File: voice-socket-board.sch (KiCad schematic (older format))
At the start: 258 parts

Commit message: changes
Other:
- note removed: "WHY IS THIS OP AMP FLIPPED OVER????"
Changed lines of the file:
@@
 F 3 "~" H 3775 14550 60  0000 C CNN
 	2    3775 14550
-	1    0    0    1
+	1    0    0    -1
 $EndComp
 $Comp
@@
 Wire Wire Line
 	20875 10525 20875 10625
-Text Notes 3650 14875 0    50   ~ 0
-WHY IS THIS OP AMP FLIPPED OVER????
 $Comp
 L R_US R?

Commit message: updated with new voice card pinout, sub oscillator added. Need to add LFO LED circuit
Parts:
- removed J?: DDR3-DIMM, MyModules:DDR3-DIMM-MO-269, symbol DDR3-DIMM
- removed R?: 10K, symbol R_US
- removed U?: CD4024BE, DIP254P762X508-14, symbol CD4024BE
- removed U?: CD4013BE, DIP254P762X508-14, symbol CD4013BE
- added C?: 0.1μ, symbol C_US
- added C?: 10p, ~, symbol C_US
- added D? (x2): 1N4148, ~, symbol DIODE
- added J?: DDR3-DIMM, MyModules:DDR3-DIMM-MO-269, symbol DDR3-DIMM
- added Q?: MMBT3904, SOT-23, symbol MMBT3904
- added R? (x2): 4.7K, symbol R_US
- added R?: 100K, ~, symbol R_US
- added R?: 68K, symbol R_US
- added R?: 220K, symbol R_US
- added R?: 33K, symbol R_US
- added R? (x2): 47K, symbol R_US
- added SW?: SP3T, symbol SP3T
- added U? (x2): 4013, symbol 4013
- added VR?: 50K, symbol POT_US
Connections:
- net labels added: 1_OCT_DOWN_SQUARE, 2_OCT_DOWN_PULSE, 2_OCT_DOWN_SQUARE, SUB_OSC
- wire segments 558 -> 723
- no-connect marks 17 -> 10
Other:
- note added: "EG2 POL"
- note added: "Ian Fritz Super Sampe & Hold"
- note added: "MIXER"
- note added: "NEED TO BREADBOARD SUB OSCILLATOR"
- note added: "QUICK & DIRTY DEBOUNCE\n"
- note added: "SH101 SUB OSCILLATOR FROM:\nhttp://electro-music.com/forum/topic-18983.html"
- note added: "SYNC SWITCH"
- note removed: "6 VPP"
- note removed: "Changed to 47K to\nprevent clipping"
- moved on the sheet: C?, R?, VR?

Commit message: added a few notes, plus LFO LED circuit
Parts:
- added D?: LED, symbol LED
- added Q?: MMBT3904, SOT-23, symbol MMBT3904
- added R?: 47K, symbol R_US
- added R?: 1K, symbol R_US
- U? (x2): value TL072- -> LM833
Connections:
- wire segments 723 -> 731
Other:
- note added: "NEED TO BREADBOARD SUB OSCILLATOR\nIT WILL HAVE +5V DC OFFSET. WILL THIS BE \nBLOCKED BY POST MIXER BLOCKING CAP?"
- note added: "OR SOME OTHER LOW OFFSET PRECISION OP AMP"
- note removed: "NEED TO BREADBOARD SUB OSCILLATOR"
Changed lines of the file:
@@
 P 13350 5775
 F 0 "U?" H 13300 5975 60  0000 L CNN
-F 1 "TL072-" H 13300 5525 60  0000 L CNN
+F 1 "LM833" H 13300 5525 60  0000 L CNN
 F 2 "" H 13350 5775 60  0000 C CNN
 F 3 "" H 13350 5775 60  0000 C CNN
@@
 P 10250 6200
 F 0 "U?" H 10200 6400 60  0000 L CNN
-F 1 "TL072-" H 10200 5950 60  0000 L CNN
+F 1 "LM833" H 10200 5950 60  0000 L CNN
 F 2 "" H 10250 6200 60  0000 C CNN
 F 3 "" H 10250 6200 60  0000 C CNN
@@
 Connection ~ 34375 7150
 Text Notes 31375 6550 0    60   ~ 0
-NEED TO BREADBOARD SUB OSCILLATOR
+NEED TO BREADBOARD SUB OSCILLATOR\nIT WILL HAVE +5V DC OFFSET. WILL THIS BE \nBLOCKED BY POST MIXER BLOCKING CAP?
 Text Notes 30875 8575 0    60   ~ 0
 SH101 SUB OSCILLATOR FROM:\nhttp://electro-music.com/forum/topic-18983.html
@@
 Wire Wire Line
 	30825 7075 30825 7100
+$Comp
+L R_US R?
+U 1 1 56680CC3
+P 21425 13100
+F 0 "R?" V 21505 13100 50  0000 C CNN
+F 1 "47K" V 21345 13100 50  0000 C CNN
+F 2 "" H 21425 13100 60  0000 C CNN
+F 3 "" H 21425 13100 60  0000 C CNN
+	1    21425 13100
+	0    1    1    0
+$EndComp
+$Comp
+L R_US R?
+U 1 1 56680CCA
+P 22175 12650
+F 0 "R?" V 22255 12650 50  0000 C CNN
+F 1 "1K" V 22095 12650 50  0000 C CNN
+F 2 "" H 22175 12650 60  0000 C CNN
+F 3 "" H 22175 12650 60  0000 C CNN
+	1    22175 12650
+	0    -1   -1   0
+$EndComp
+$Comp
+L GND_E #PWR?
+U 1 1 56680CD1
+P 23025 12950
+F 0 "#PWR?" V 23025 12950 30  0001 C CNN
+F 1 "GND_E" H 23025 12880 30  0001 C CNN
+F 2 "~" H 23025 12950 60  0000 C CNN
+F 3 "~" H 23025 12950 60  0000 C CNN
+	1    23025 12950
+	1    0    0    -1
+$EndComp
+Wire Wire Line
+	21575 12650 21425 12650
+Wire Wire Line
+	23025 12650 23025 12950
+Wire Wire Line
+	22825 12650 23025 12650
+Wire Wire Line
+	21775 13100 21775 12950
+Wire Wire Line
+	21625 13100 21775 13100
+Wire Wire Line
+	21225 13100 21125 13100
+Wire Wire Line
+	21425 12650 21425 12450
+$Comp
+L MMBT3904 Q?
+U 1 1 566845D9
+P 21775 12750
+F 0 "Q?" H 21975 12825 50  0000 L CNN
+F 1 "MMBT3904" H 21975 12750 50  0000 L CNN
+F 2 "SOT-23" H 21975 12675 50  0001 L CIN
+F 3 "" H 21775 12750 50  0000 L CNN
+	1    21775 12750
+	0    -1   -1   0
+$EndComp
+$Comp
+L LED D?
+U 1 1 56688E5A
+P 22625 12650
+F 0 "D?" H 22625 12750 50  0000 C CNN
+F 1 "LED" H 22625 12550 50  0000 C CNN
+F 2 "" H 22625 12650 60  0000 C CNN
+F 3 "" H 22625 12650 60  0000 C CNN
+	1    22625 12650
+	-1   0    0    1
+$EndComp
+Wire Wire Line
+	22375 12650 22425 12650
+$Comp
+L +12V #PWR?
+U 1 1 56691909
+P 21425 12450
+F 0 "#PWR?" H 21425 12300 50  0001 C CNN
+F 1 "+12V" H 21425 12590 50  0000 C CNN
+F 2 "" H 21425 12450 60  0000 C CNN
+F 3 "" H 21425 12450 60  0000 C CNN
+	1    21425 12450
+	-1   0    0    -1
+$EndComp
+Connection ~ 9750 6200
+Text Notes 13400 6150 0    50   ~ 0
+OR SOME OTHER LOW OFFSET PRECISION OP AMP
 $EndSCHEMATC

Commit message: just made DDR3 DIMM connector footprint. 240 pins. Phew.
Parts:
- removed C? (x2): 470n, ~, symbol C_US
- removed C?: 0.1μ, symbol C_US
- removed J?: JACK_MONO_SW, symbol JACK_MONO_SW
- removed Q?: BCM857BS, ~, symbol BCM857BS
- removed R? (x4): 4.7K, ~, symbol R_US
- removed R? (x2): 100K, symbol R_US
- removed R?: 39K, ~, symbol R_US
- removed R?: 33K, symbol R_US
- removed R?: 1K 3300ppm/K, ~, symbol R_TEMPCO
- removed R? (x2): 4.7K, symbol R_US
- removed SW? (x2): SPST, symbol SPST
- removed TP? (x2): CONN_1, ~, symbol CONN_1
- removed U? (x2): LM13700, ~, symbol LM13700
- removed U? (x2): TL072-, ~, symbol TL072-
- removed VR?: 50K, symbol POT_US
- added C?: 470n, ~, symbol C_US
- added C? (x2): 10μF, MyModules:2MM-POL-CAP, symbol CP_US
- added C? (x10): 100n, MyModules:SM0603-C-JRL, symbol C_US
- added J?: JACK_MONO_SW, symbol JACK_MONO_SW
- added P? (x2): CONN_01X03, symbol CONN_01X03
- added P?: CONN_02X05, Pin_Headers:Pin_Header_Straight_2x05, symbol CONN_02X05
- added R?: 100K, symbol R_US
- added R? (x6): 47K, symbol R_US
- added R?: 1meg, symbol R_US
- added R? (x2): 100, symbol R_US
- added R?: 10K, symbol R_US
- added SW?: SP3T, symbol SP3T
- added SW? (x2): SPST, symbol SPST
- added TP?: CONN_1, ~, symbol CONN_1
- added U? (x2): TL072-, ~, symbol TL072-
- added U? (x2): TL072-, symbol TL072-
- added VR?: 1meg LOG, symbol POT_US
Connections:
- net labels added: KEY_TRACK
- wire segments 731 -> 1002
- no-connect marks 10 -> 8
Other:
- note added: "DECOUPLING"
- note added: "JUMPER"
- note added: "NORM"
- note added: "SIMPLE SLEW FROM:\nhttp://4.bp.blogspot.com/_UZMTRL9r8vU/TTGv3KWKT1I/AAAAAAAAAGw/SQU2PrACBgo/s1600/slew.jpg\nhttp://synovatron.blogspot.co.uk/p/cv-tools-project.html"
- note added: "VCF KEY\nTRACKING\n"
- note added: "WIDE"
- note removed: "*NOTE: C47 and C48 values: need\nto experiment more with C47 and \nC48 values. Changee to dual\nfootprint 0805 and TH."
- note removed: "ADAPTED FROM SCI PROPHET 5 GLIDE CIRCUIT"
- note removed: "GLIDE\n"
- moved on the sheet: R?

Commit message: annotated, doing ERC now
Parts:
- removed J?: JACK_MONO_SW, symbol JACK_MONO_SW
- removed Q? (x2): DMMT3904, symbol DMMT3904
- removed R?: 10K, symbol R_US
- removed VR?: POT_US, symbol POT_US
- added Q2: DMMT3904W, SOT-23, symbol DMMT3904W
- added R12, R7: 100K, symbol R_US
- gave numbers to parts that had none: 273
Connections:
- net +12V: no longer U5.8 (V+)
- net -12V: no longer U5.4 (V-)
- net VCO1_OCTAVE: now also R7.2
- net VCO1_PITCH_CV: now also R13.1, R12.1, R7.1
- net VCO2_OCTAVE: now also R12.2
- net at D3.2 (K), R58.2, R59.1: now also U4.3 (+); no longer U4.5 (+)
- net at R56.1, R57.1: now also U4.2 (-); no longer U4.6 (-)
- net at D5.1 (A), Q3.2 (G), Q3.5 (G): now also U4.1; no longer U4.7
- net at C16.2, R63.1: now also Q2.5 (E)
- net at C18.1 (+), R65.1: now also Q2.3 (C)
- net at C17.1 (+), R66.1: now also Q2.4 (E)
- net at R62.2: now also U5.6 (-); no longer U5.2 (-)
- net at P2.3 (P3), R60.1: now also U5.7; no longer U5.1
- net at R54.2, R55.2: now also U5.5 (+); no longer U5.3 (+)
- net 1_OCT_DOWN_SQUARE: no longer names the net of D7.1 (A), R83.2, SW10.1
- net 2_OCT_DOWN_PULSE: no longer names the net of D6.2 (K), D7.2 (K), SW10.4
- net 2_OCT_DOWN_SQUARE: no longer names the net of D6.1 (A), R82.2, SW10.2
- new net: Q2.1 (B), Q2.2 (B)
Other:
- note added: "1_OCT_DOWN_SQUARE"
- note added: "2_OCT_DOWN_PULSE"
- note added: "2_OCT_DOWN_SQUARE"
- moved on the sheet: C1, C10, C11, C12, C13, C14, C15, C16, C17, C18, C19, C2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

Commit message: starting footprint assignment. added .gitingore
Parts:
- removed U10: TL074-, ~, symbol TL074-
- added unit 2 of U10
- VR10: renamed from VR16; value POT_US -> 50K
- VR11: renamed from VR17; value POT_US -> 50K
- VR12: renamed from VR18; value POT_US -> 50K
- VR13: renamed from VR19; value POT_US -> 50K
- VR14: renamed from VR20; value POT_US -> 50K
- VR7: renamed from VR13; value POT_US -> 50K
- VR8: renamed from VR14; value POT_US -> 50K
- VR9: renamed from VR15; value POT_US -> 50K
- renumbered J4 to J2, J2 to P4, VR6 to TR4, VR8 to TR5, VR7 to TR6, VR9 to TR7, VR10 to TR8, VR11 to TR9, U11 to U10, U12 to U11, VR21 to VR15, VR22 to VR16, VR25 to VR17, VR27 to VR18, VR26 to VR19, VR28 to VR20, VR23 to VR21, VR24 to VR22, VR29 to VR23, VR30 to VR24, VR31 to VR25, VR32 to VR26, VR12 to VR6
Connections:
- net +12V: now also U4.8 (V+)
- net -12V: now also U4.4 (V-)
- net EG1_ATTACK_CV: now also VR7.2
- net EG1_DECAY_CV: now also VR9.2
- net EG1_RELEASE_CV: now also VR13.2
- net EG1_SUSTAIN_CV: now also VR11.2
- net EG2_ATTACK_CV: now also VR8.2
- net EG2_DECAY_CV: now also VR10.2
- net EG2_RELEASE_CV: now also VR14.2
- net EG2_SUSTAIN_CV: now also VR12.2
- net GND: now also U10.5 (+)
- net at C57.2, R102.1, TP4.1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: now also U10.7
- net at C57.1, R100.1, R101.1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: now also U10.6 (-)
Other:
- moved on the sheet: C10, C11, C12, C13, C6, C7, R32, R33, R34, R35, R40, R41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

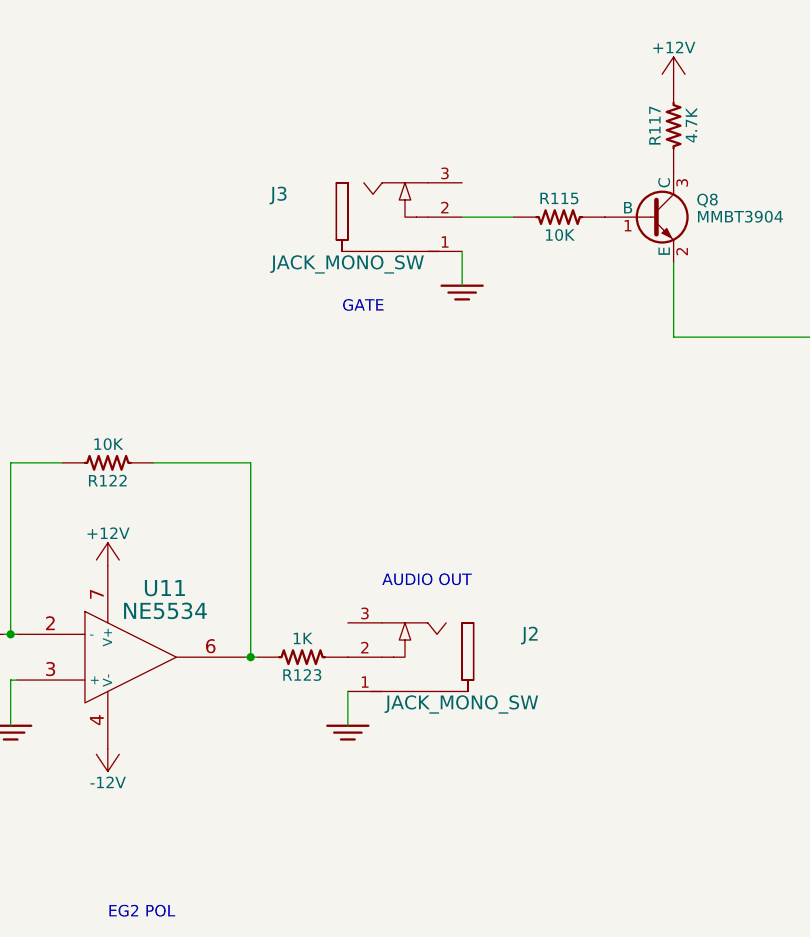
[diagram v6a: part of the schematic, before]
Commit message: almost done assigning footprints. Need to pay close attention to 3mm LEDs and 1N4148 SOD323 diode packages as the anode and cathodes were swapped in the more recent versions of Kicad
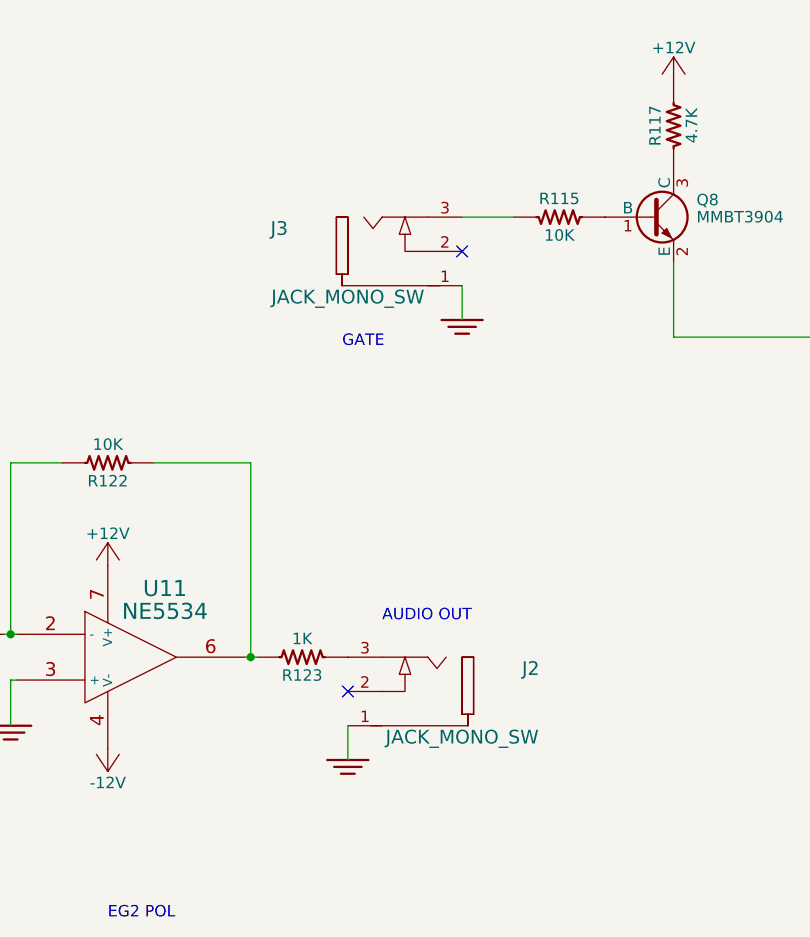
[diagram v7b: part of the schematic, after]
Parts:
- C1, C15, C2, C27, C28, C31, C32, C37, C38, C39, C40, C41, C42, C45, C46, C47, C48, C49, C50, C51, C52, C54, C57, C58, C59, C60: footprint ~ -> MyModules:SM0603-C-JRL
- C10, C11, C12, C13, C14, C16, C19, C20, C21, C22, C3, C4, C53, C55, C56, C6, C7, C8, C9: footprint (none) -> MyModules:SM0603-C-JRL
- C17, C18: footprint (none) -> MyModules:2MM-POL-CAP
- C5, C61: footprint ~ -> MyModules:SM0805-HAND
- D1, D2: footprint (none) -> MyModules:SOT23-JRL
- D3, D5, D6, D7, D8: footprint ~ -> MyModules:SOD323-JRL
- D4, D9: footprint (none) -> MyModules:3MM-LED-C1A2
- P3: footprint Pin_Headers:Pin_Header_Straight_2x05 -> (none)
- P4: footprint MyModules:DDR3-DIMM-MO-269 -> (none)
- Q1, Q2, Q5, Q7, Q8, Q9: footprint SOT-23 -> (none)
- Q6, R105, R106, R107, R108, R109, R110, R111, R112, R113, TR1, TR2, TR3, U10, U2, U9: footprint ~ -> (none)
- SW1, SW14, SW2, SW5, SW6, SW7: footprint (none) -> MyModules:SS-12F45-1P2T-SLIDE
- SW10, SW11, SW12, SW13, SW3, SW4, SW8, SW9: footprint (none) -> MyModules:SS-23E02-2P3T-SLIDE
- TP1, TP2, TP3, TP4, TP5: footprint ~ -> MyModules:TEST_POINT_LOOP_4592
- U11, U7: footprint Housings_SSOP:MSOP-8_3x3mm_Pitch0.65mm -> (none)
- VR1, VR10, VR11, VR12, VR13, VR14, VR15, VR16, VR17, VR18, VR19, VR2, VR20, VR21, VR22, VR23, VR24, VR25, VR26, VR3, VR4, VR5, VR6, VR7, VR8, VR9: footprint (none) -> MyModules:RV09AF-40-ALPHA-POT
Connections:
- net at J2.2: no longer R123.1
- net at J2.3: now also R123.1
- net at J3.2: no longer R115.1
- net at J3.3: now also R115.1
- no-connect marks 8 -> 10
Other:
- moved on the sheet: J2, J3

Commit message: footprints assigned. about to start PCB
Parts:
- J1, J2, J3: footprint (none) -> MyModules:PJ-301B-JACK-SLOTS
- P1, P2: footprint (none) -> Pin_Headers:Pin_Header_Straight_1x03
- P3: footprint (none) -> Pin_Headers:Pin_Header_Straight_2x05
- P4: footprint (none) -> MyModules:DDR3-DIMM-240-FCI
- Q1, Q5, Q6, Q7, Q8, Q9: footprint (none) -> MyModules:SOT23-JRL
- Q2, Q3, Q4: footprint (none) -> MyModules:SOT363-JRL
- R1, R10, R100, R101, R102, R103, R104, R105, R106, R107, R108, R109, R11, R110, R111, R112, R113, R114, R115, R116, R117, R118, R119, R12, R120, R121, R122, R123, R13, R14, R15, R16, R17, R18, R19, R2, R20, R21, R22, R23, R24, R25, R26, R27, R28, R29, R3, R30, R31, R32, R33, R34, R35, R36, R37, R38, R39, R4, R40, R41, R42, R43, R44, R45, R46, R47, R48, R49, R5, R50, R51, R52, R53, R54, R55, R56, R57, R58, R59, R6, R60, R61, R62, R63, R64, R65, R66, R67, R68, R69, R7, R70, R71, R72, R73, R74, R75, R76, R77, R78, R79, R8, R80, R81, R82, R83, R84, R85, R86, R87, R88, R89, R9, R90, R91, R92, R93, R94, R95, R96, R97, R98, R99: footprint (none) -> MyModules:SM0603-R-JRL
- SW15: footprint (none) -> Buttons_Switches_ThroughHole:SW_PUSH-12mm
- TR1, TR2, TR3, TR6, TR8: footprint (none) -> MyModules:Bourns_3362P
- TR10: renamed from VR16; footprint MyModules:RV09AF-40-ALPHA-POT -> MyModules:Bourns_3362P
- TR4, TR5, TR7, TR9: footprint (none) -> MyModules:Bourns-3296W
- U1, U10, U2, U3, U4, U5, U6, U9: footprint (none) -> MyModules:TSSOP8-JRL
- U11: footprint (none) -> Housings_SOIC:SOIC-8_3.9x4.9mm_Pitch1.27mm
- U7: footprint (none) -> Housings_SSOP:MSOP-8_3x3mm_Pitch0.65mm
- U8: value 4013 -> CD4013; footprint (none) -> Housings_SSOP:TSSOP-14_4.4x5mm_Pitch0.65mm
- renumbered VR17 to VR16, VR18 to VR17, VR19 to VR18, VR20 to VR19, VR21 to VR20, VR22 to VR21, VR23 to VR22, VR24 to VR23, VR25 to VR24, VR26 to VR25
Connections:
- no-connect marks 10 -> 12
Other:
- note added: "SOT23 PINS\nCONFIRMED"
